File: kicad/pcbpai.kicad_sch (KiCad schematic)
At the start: 20 parts, among them J1 Fuse, J10 Conn_01x02_Socket, J11 Conn_01x02_Socket, J12 Conn_01x02_Socket, J2 Conn_01x08_Socket, J3 Input 24 V, J4 Boton Encendido, J5 Parada de Emergencia, J6 Conn_01x08_Socket, J7 Raspberry GPIO, J8 Conn_01x02_Socket, J9 Conn_01x02_Socket, U6 ATtiny85-20P

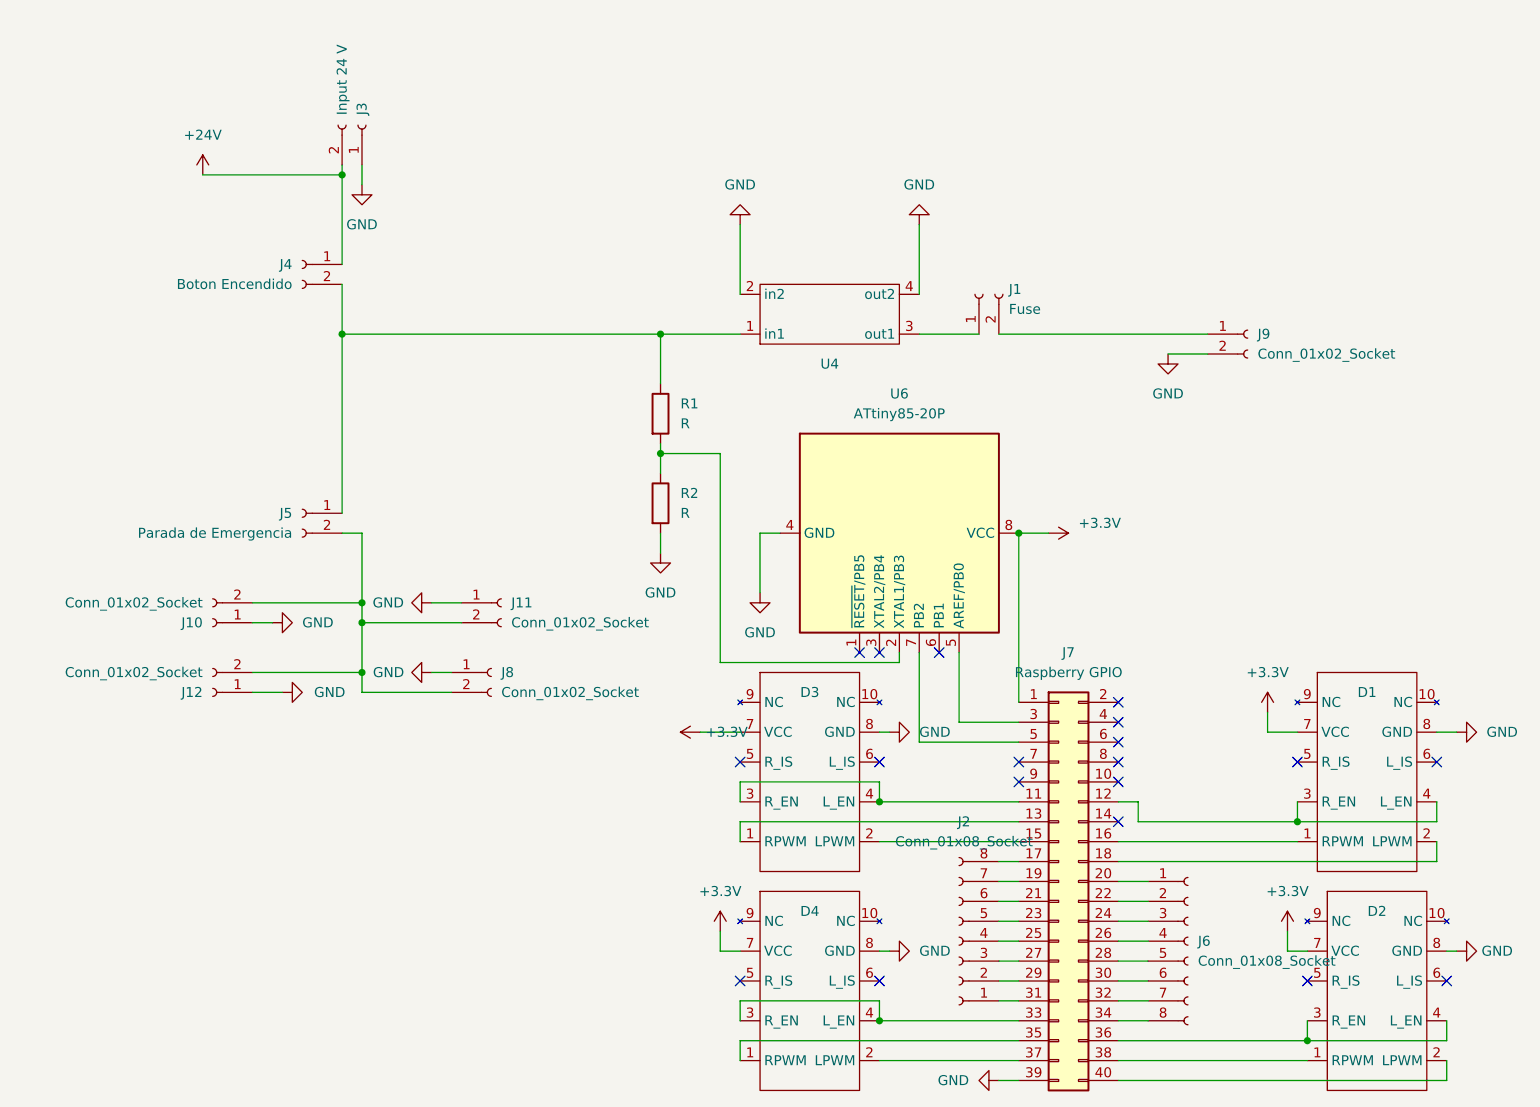
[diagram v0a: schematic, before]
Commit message: change switch and fuse symbols
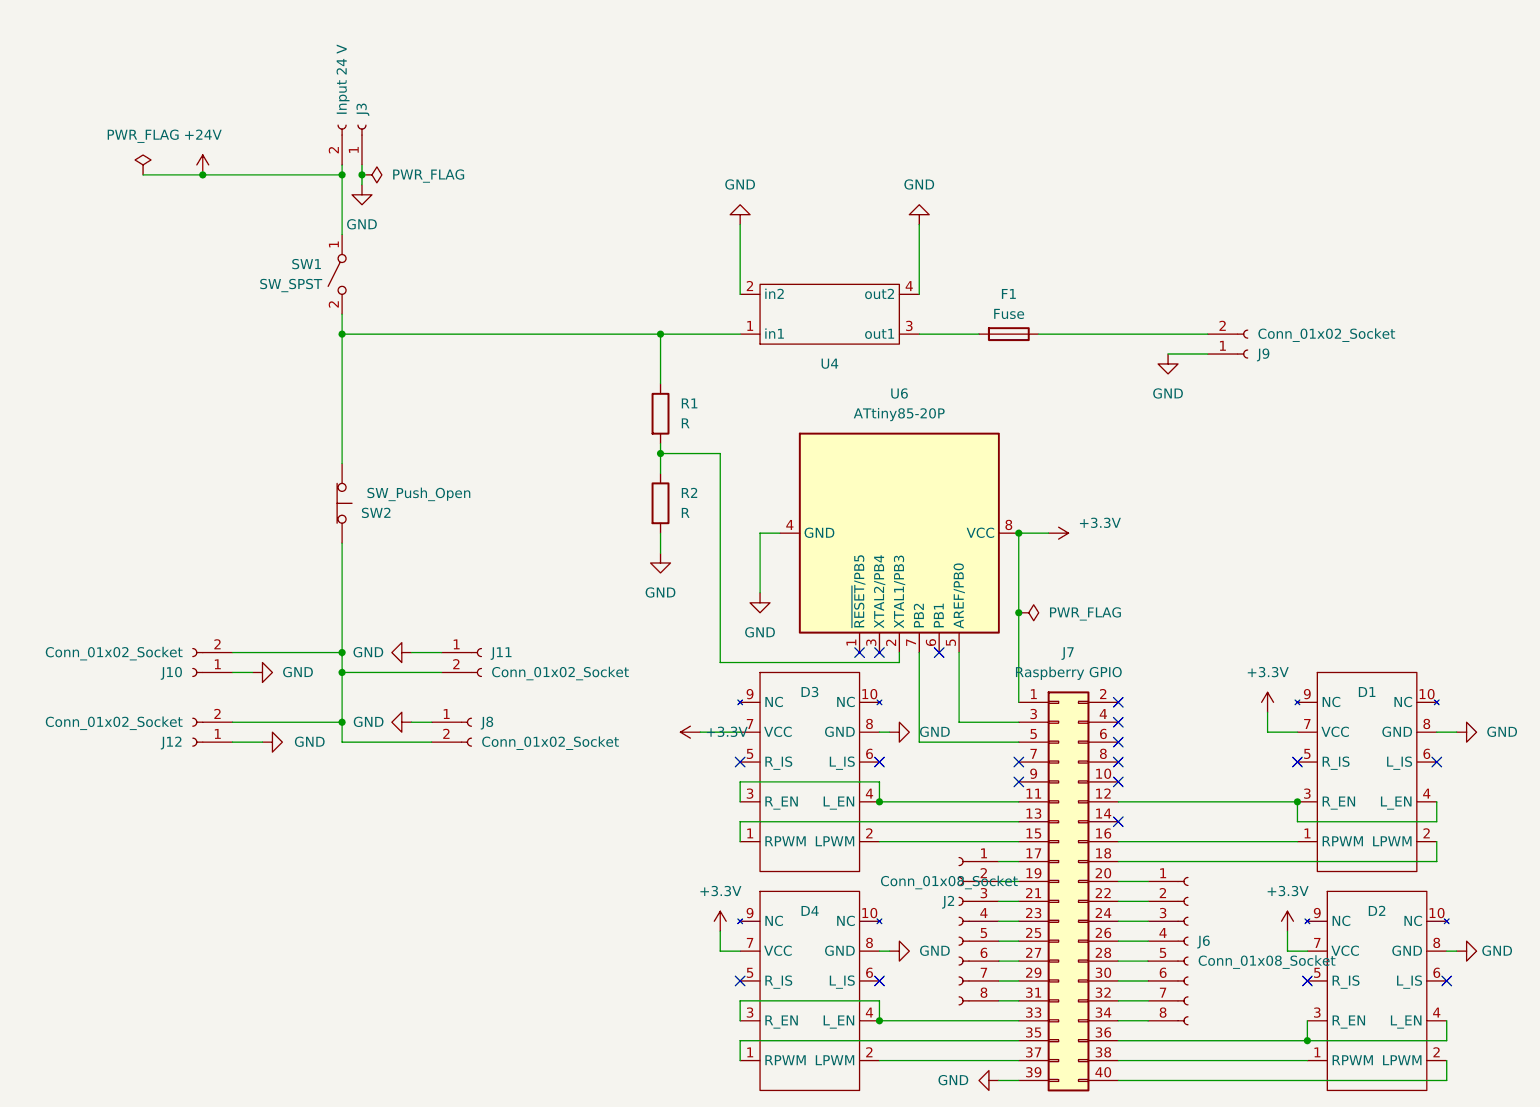
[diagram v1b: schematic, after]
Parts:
- removed J1: Fuse, PAI:fuse, symbol Connector:Conn_01x02_Socket
- removed J4: Boton Encendido, Connector_Phoenix_MSTB:PhoenixContact_MSTBA_2,5_2-G_1x02_P5.00mm_Horizontal, symbol Connector:Conn_01x02_Socket
- removed J5: Parada de Emergencia, Connector_Phoenix_MSTB:PhoenixContact_MSTBA_2,5_2-G_1x02_P5.00mm_Horizontal, symbol Connector:Conn_01x02_Socket
- added F1: Fuse, PAI:fuse, symbol Device:Fuse
- added SW1: SW_SPST, Connector_Phoenix_MSTB:PhoenixContact_MSTBA_2,5_2-G_1x02_P5.00mm_Horizontal, symbol Switch:SW_SPST
- added SW2: SW_Push_Open, Connector_Phoenix_MSTB:PhoenixContact_MSTBA_2,5_2-G_1x02_P5.00mm_Horizontal, symbol Switch:SW_Push_Open
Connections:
- net +24V: now also SW1.1 (A)
- net GND: now also J9.1 (Pin_1); no longer J9.2 (Pin_2)
- net at R1.1, U4.1 (in1): now also SW1.2 (B), SW2.1 (A)
- net at J10.2 (Pin_2), J11.2 (Pin_2), J12.2 (Pin_2)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: now also SW2.2 (B)
- net at U4.3 (out1): now also F1.2
- net at J2.1 (Pin_1): now also J7.17 (Pin_17); no longer J7.31 (Pin_31)
- net at J2.2 (Pin_2): now also J7.19 (Pin_19); no longer J7.29 (Pin_29)
- net at J2.3 (Pin_3): now also J7.21 (Pin_21); no longer J7.27 (Pin_27)
- net at J2.4 (Pin_4): now also J7.23 (Pin_23); no longer J7.25 (Pin_25)
- net at J2.5 (Pin_5): now also J7.25 (Pin_25); no longer J7.23 (Pin_23)
- net at J2.6 (Pin_6): now also J7.27 (Pin_27); no longer J7.21 (Pin_21)
- net at J2.7 (Pin_7): now also J7.29 (Pin_29); no longer J7.19 (Pin_19)
- net at J2.8 (Pin_8): now also J7.31 (Pin_31); no longer J7.17 (Pin_17)
- new net: F1.1, J9.2 (Pin_2)
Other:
- moved on the sheet: J10, J11, J12, J2, J8
